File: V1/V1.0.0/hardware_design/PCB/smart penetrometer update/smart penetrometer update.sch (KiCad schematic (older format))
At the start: 25 parts, among them J1 XLR3_Switched, J2 Conn_01x11_Female, U1 4001, U2 DS3231M, U3 Battery_Input, U4 4023, U5 ADS1115IDGS, U6 3v3_Voltage_Regulator, U7 Solar_Input

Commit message: code update
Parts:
- A1: symbol smart-penetrometer-rescue:SD_Card_Module-Charleslabs_Parts-kitest-rescue -> smart-penetrometer-update-rescue:SD_Card_Module-Charleslabs_Parts-kitest-rescue-smart-penetrometer-rescue
- A2: symbol smart-penetrometer-rescue:Arduino_Nano_v3.x-MCU_Module-kitest-rescue -> smart-penetrometer-update-rescue:Arduino_Nano_v3.x-MCU_Module-kitest-rescue-smart-penetrometer-rescue
- U3, U7: symbol smart-penetrometer-rescue:Battery_Input-kitest-kitest-rescue -> smart-penetrometer-update-rescue:Battery_Input-kitest-kitest-rescue-smart-penetrometer-rescue
- U6: symbol smart-penetrometer-rescue:3v3_Voltage_Regulator -> smart-penetrometer-update-rescue:3v3_Voltage_Regulator-smart-penetrometer-rescue
- U?: symbol smart-penetrometer-rescue:DW01 -> smart-penetrometer-update-rescue:DW01-smart-penetrometer-rescue
- U?: symbol smart-penetrometer-rescue:FS8205A -> smart-penetrometer-update-rescue:FS8205A-smart-penetrometer-rescue
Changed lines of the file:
@@
 NoConn ~ 4850 4450
 $Comp
-L smart-penetrometer-rescue:Battery_Input-kitest-kitest-rescue U3
+L smart-penetrometer-update-rescue:Battery_Input-kitest-kitest-rescue-smart-penetrometer-rescue U3
 U 1 1 60A6877D
 P 4200 750
@@
 $EndComp
 $Comp
-L smart-penetrometer-rescue:Arduino_Nano_v3.x-MCU_Module-kitest-rescue A2
+L smart-penetrometer-update-rescue:Arduino_Nano_v3.x-MCU_Module-kitest-rescue-smart-penetrometer-rescue A2
 U 1 1 60A40C30
 P 5350 4150
@@
 $EndComp
 $Comp
-L smart-penetrometer-rescue:SD_Card_Module-Charleslabs_Parts-kitest-rescue A1
+L smart-penetrometer-update-rescue:SD_Card_Module-Charleslabs_Parts-kitest-rescue-smart-penetrometer-rescue A1
 U 1 1 60A4A816
 P 5350 2750
@@
 $EndComp
 $Comp
-L smart-penetrometer-rescue:3v3_Voltage_Regulator U6
+L smart-penetrometer-update-rescue:3v3_Voltage_Regulator-smart-penetrometer-rescue U6
 U 1 1 61FF42DE
 P 2650 2600
@@
 $EndComp
 $Comp
-L smart-penetrometer-rescue:Battery_Input-kitest-kitest-rescue U7
+L smart-penetrometer-update-rescue:Battery_Input-kitest-kitest-rescue-smart-penetrometer-rescue U7
 U 1 1 62051BA4
 P 3400 1950
@@
 $EndComp
 $Comp
-L smart-penetrometer-rescue:DW01 U?
+L smart-penetrometer-update-rescue:DW01-smart-penetrometer-rescue U?
 U 1 1 62805E03
 P 4300 1450
@@
 	4050 900  4050 1200
 $Comp
-L smart-penetrometer-rescue:FS8205A U?
+L smart-penetrometer-update-rescue:FS8205A-smart-penetrometer-rescue U?
 U 1 1 62819888
 P 2600 1250

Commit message: schematic update
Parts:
- removed U1: 4001, kitest:uofsc_logo_1in, symbol 4xxx:4001
- added C? (x2): C_0.047uF, symbol Device:C_Small
- added C?: C_0.47uF, symbol Device:C_Small
- added C? (x2): C_0.1uF, symbol Device:C_Small
- added R? (x2): R_800Ohm, symbol Device:R_Small_US
- added R? (x2): R_1MOhm, symbol Device:R_Small_US
- added U?: ADS1120-PW, Package_SO:TSSOP-16_4.4x5mm_P0.65mm, symbol Analog_ADC:ADS1120-PW
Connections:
- net labels added: Earth
- wire segments 121 -> 147
- no-connect marks 30 -> 31

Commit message: SCHEMATIC UPDAYE
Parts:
- added U?: SRAM(23K256), symbol smart-penetrometer-update-rescue:SRAM(23K256)
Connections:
- net GND: now also U?.4 (VSS)
- net at A2.10 (D7): now also U?.7 (HOLD)
- net at A2.11 (D8): now also U?.1 (CS)
- net at A1.3 (MOSI), A2.14 (D11), U?.16 (DIN): now also U?.5 (SI)
- net at A1.5 (MISO), A2.15 (D12), U?.15 (DOUT/~DRDY): now also U?.2 (SO)
- net at A1.4 (CLK), A2.16 (D13), U?.1 (SCLK): now also U?.6 (SCK)
- net at A1.1 (3V3), A2.30 (VIN), C2.2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: now also U?.8 (VCC)
- no-connect marks 31 -> 29
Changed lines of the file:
@@
 NoConn ~ 4850 4050
 NoConn ~ 4850 4150
-NoConn ~ 4850 4250
-NoConn ~ 4850 4350
 $Comp
 L smart-penetrometer-update-rescue:Battery_Input-kitest-kitest-rescue-smart-penetrometer-rescue U3
@@
 	1    0    0    -1
 $EndComp
-$Comp
-L Analog_ADC:ADS1115IDGS U5
-U 1 1 615B81A7
-P 5150 6300
-F 0 "U5" H 5150 6981 50  0000 C CNN
-F 1 "ADS1115IDGS" H 5150 6890 50  0000 C CNN
-F 2 "Package_SO:TSSOP-10_3x3mm_P0.5mm" H 5150 5800 50  0001 C CNN
-F 3 "http://www.ti.com/lit/ds/symlink/ads1113.pdf" H 5100 5400 50  0001 C CNN
-	1    5150 6300
-	1    0    0    -1
-$EndComp
 Wire Wire Line
 	5550 6300 5950 6300
@@
 U 1 1 6162D30F
 P 6050 3200
-F 0 "R5" H 6118 3246 50  0000 L CNN
-F 1 "R_Small_US" H 6118 3155 50  0000 L CNN
+F 0 "R5" H 6000 3350 50  0000 L CNN
+F 1 "R_Small_US" V 5950 2850 50  0000 L CNN
 F 2 "Resistor_SMD:R_1206_3216Metric" H 6050 3200 50  0001 C CNN
 F 3 "~" H 6050 3200 50  0001 C CNN
@@
 U 1 1 6162E2E0
 P 6150 3200
-F 0 "R6" H 6150 3050 50  0000 L CNN
-F 1 "R_Small_US" H 6218 3155 50  0000 L CNN
+F 0 "R6" H 6100 3350 50  0000 L CNN
+F 1 "R_Small_US" V 6250 2850 50  0000 L CNN
 F 2 "Resistor_SMD:R_1206_3216Metric" H 6150 3200 50  0001 C CNN
 F 3 "~" H 6150 3200 50  0001 C CNN
@@
 U 1 1 6163E9E6
 P 6850 3350
-F 0 "C4" V 6621 3350 50  0000 C CNN
-F 1 "C_Small" V 6712 3350 50  0000 C CNN
+F 0 "C4" V 6950 3450 50  0000 C CNN
+F 1 "C_Small" V 7000 3450 50  0000 C CNN
 F 2 "Capacitor_SMD:C_1206_3216Metric" H 6850 3350 50  0001 C CNN
 F 3 "~" H 6850 3350 50  0001 C CNN
@@
 P 6950 3350
 F 0 "#PWR011" H 6950 3100 50  0001 C CNN
-F 1 "GNDS" V 6955 3222 50  0000 R CNN
+F 1 "GNDS" V 6950 3150 50  0000 R CNN
 F 2 "" H 6950 3350 50  0001 C CNN
 F 3 "" H 6950 3350 50  0001 C CNN
@@
 U 1 1 61FFB484
 P 2900 2850
-F 0 "C2" V 2992 2896 50  0000 L CNN
-F 1 "C_10uF" V 3100 2800 50  0000 L CNN
+F 0 "C2" V 2850 3100 50  0000 L CNN
+F 1 "C_10uF" V 2950 3050 50  0000 L CNN
 F 2 "Capacitor_SMD:C_1206_3216Metric" H 2900 2850 50  0001 C CNN
 F 3 "~" H 2900 2850 50  0001 C CNN
@@
 U 1 1 62002596
 P 2400 3100
-F 0 "D1" H 2450 3200 50  0000 C CNN
-F 1 "D_Zener_Small" H 2400 3300 50  0000 C CNN
+F 0 "D1" H 2800 3050 50  0000 C CNN
+F 1 "D_Zener_Small" H 2800 3100 50  0000 C CNN
 F 2 "Diode_SMD:D_SMC" V 2400 3100 50  0001 C CNN
 F 3 "~" V 2400 3100 50  0001 C CNN
@@
 $EndComp
 Wire Wire Line
-	4700 6300 4700 6950
-Wire Wire Line
 	4700 6950 6400 6950
 Wire Wire Line
@@
 Wire Wire Line
 	4650 6200 4650 7000
-Wire Wire Line
-	4650 7000 6350 7000
 Wire Wire Line
 	6350 7000 6350 5950
@@
 P 3400 1950
 F 0 "U7" H 3658 1984 50  0000 L CNN
-F 1 "Solar_Input" H 3250 2150 50  0000 L CNN
+F 1 "Solar_Input" H 2750 2000 50  0000 L CNN
 F 2 "kitest:Battery_Input" H 3400 1950 50  0001 C CNN
 F 3 "" H 3400 1950 50  0001 C CNN
@@
 P 2300 3100
 F 0 "#PWR0106" H 2300 2850 50  0001 C CNN
-F 1 "GND" H 2305 2927 50  0000 C CNN
+F 1 "GND" H 2300 2950 50  0000 C CNN
 F 2 "" H 2300 3100 50  0001 C CNN
 F 3 "" H 2300 3100 50  0001 C CNN
@@
 P 2300 2850
 F 0 "#PWR0107" H 2300 2600 50  0001 C CNN
-F 1 "GND" H 2305 2677 50  0000 C CNN
+F 1 "GND" H 2300 2700 50  0000 C CNN
 F 2 "" H 2300 2850 50  0001 C CNN
 F 3 "" H 2300 2850 50  0001 C CNN
@@
 U 1 1 6280EF6A
 P 4300 1800
-F 0 "R?" H 4368 1846 50  0000 L CNN
+F 0 "R?" H 4500 1800 50  0000 L CNN
 F 1 "R_Small_US" H 4368 1755 50  0000 L CNN
 F 2 "" H 4300 1800 50  0001 C CNN
@@
 U 1 1 6280FAAE
 P 4350 1100
-F 0 "R?" H 4418 1146 50  0000 L CNN
+F 0 "R?" H 4550 1100 50  0000 L CNN
 F 1 "R_Small_US" H 4418 1055 50  0000 L CNN
 F 2 "" H 4350 1100 50  0001 C CNN
@@
 U 1 1 62819F8F
 P 4200 1000
-F 0 "C?" V 4428 1000 50  0000 C CNN
-F 1 "CP1_Small" V 4337 1000 50  0000 C CNN
+F 0 "C?" V 4300 1000 50  0000 C CNN
+F 1 "CP1_Small" V 4250 1400 50  0000 C CNN
 F 2 "" H 4200 1000 50  0001 C CNN
 F 3 "~" H 4200 1000 50  0001 C CNN
@@
 	2250 4250 2250 4450
 Wire Wire Line
-	2800 3100 3500 3100
+	2800 3100 3450 3100
 Connection ~ 2350 4250
 Connection ~ 2250 4450
@@
 	950  4250 950  4750
 Connection ~ 2250 4250
+$Comp
+L smart-penetrometer-update-rescue:SRAM(23K256) U?
+U 1 1 62EB656F
+P 2500 6900
+F 0 "U?" H 2500 7465 50  0000 C CNN
+F 1 "SRAM(23K256)" H 2500 7374 50  0000 C CNN
+F 2 "" H 2500 6900 50  0001 C CNN
+F 3 "" H 2500 6900 50  0001 C CNN
+	1    2500 6900
+	1    0    0    -1
+$EndComp
+Wire Wire Line
+	2800 6600 3450 6600
+Wire Wire Line
+	3450 6600 3450 3100
+Connection ~ 3450 3100
+Wire Wire Line
+	3450 3100 3500 3100
+$Comp
+L power:GND #PWR?
+U 1 1 62FCEB65
+P 2200 7200
+F 0 "#PWR?" H 2200 6950 50  0001 C CNN
+F 1 "GND" H 2205 7027 50  0000 C CNN
+F 2 "" H 2200 7200 50  0001 C CNN
+F 3 "" H 2200 7200 50  0001 C CNN
+	1    2200 7200
+	1    0    0    -1
+$EndComp
+$Comp
+L Analog_ADC:ADS1115IDGS U5
+U 1 1 615B81A7
+P 5150 6300
+F 0 "U5" H 5150 6981 50  0000 C CNN
+F 1 "ADS1115IDGS" H 5150 6890 50  0000 C CNN
+F 2 "Package_SO:TSSOP-10_3x3mm_P0.5mm" H 5150 5800 50  0001 C CNN
+F 3 "http://www.ti.com/lit/ds/symlink/ads1113.pdf" H 5100 5400 50  0001 C CNN
+	1    5150 6300
+	1    0    0    -1
+$EndComp
+Wire Wire Line
+	4700 6300 4700 6950
+Wire Wire Line
+	4650 7000 6350 7000
+Wire Wire Line
+	4750 4900 4750 6050
+Wire Wire Line
+	4750 6050 3650 6050
+Wire Wire Line
+	3650 6050 3650 7000
+Wire Wire Line
+	3650 7000 2800 7000
+Connection ~ 4750 4900
+Wire Wire Line
+	4700 5000 4700 6000
+Wire Wire Line
+	4700 6000 3700 6000
+Wire Wire Line
+	3700 6000 3700 7200
+Wire Wire Line
+	3700 7200 2800 7200
+Connection ~ 4700 5000
+Wire Wire Line
+	4800 5100 4800 6100
+Wire Wire Line
+	4800 6100 2100 6100
+Wire Wire Line
+	2100 6100 2100 6800
+Wire Wire Line
+	2100 6800 2200 6800
+Connection ~ 4800 5100
+Wire Wire Line
+	2200 6600 2200 5950
+Wire Wire Line
+	2200 5950 4550 5950
+Wire Wire Line
+	4550 5950 4550 4350
+Wire Wire Line
+	4550 4350 4850 4350
+Wire Wire Line
+	2800 6800 3600 6800
+Wire Wire Line
+	3600 6800 3600 5900
+Wire Wire Line
+	3600 5900 4500 5900
+Wire Wire Line
+	4500 5900 4500 4250
+Wire Wire Line
+	4500 4250 4850 4250
 $EndSCHEMATC

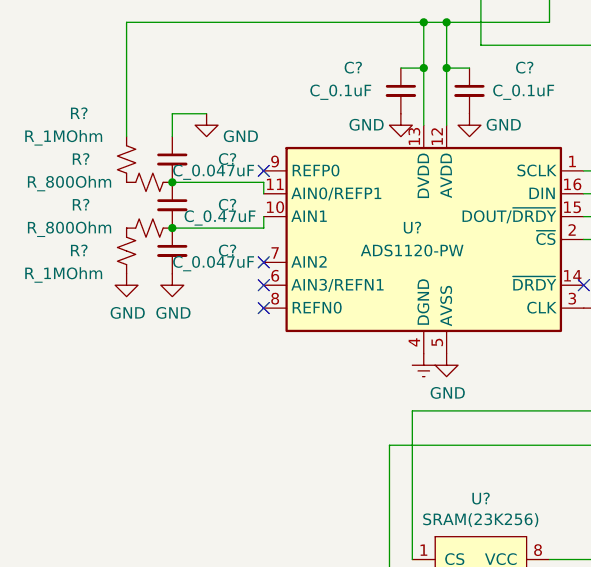
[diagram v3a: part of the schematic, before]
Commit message: schematic update
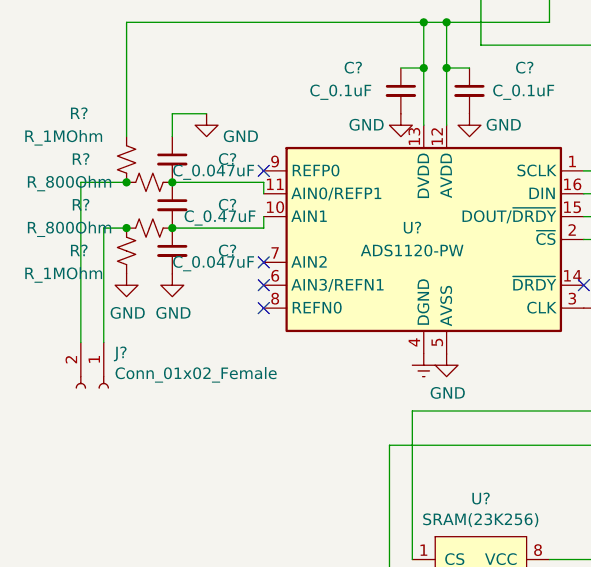
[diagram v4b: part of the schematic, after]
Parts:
- added J?: Conn_01x02_Female, symbol Connector:Conn_01x02_Female
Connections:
- net at R?.2, R?.2: now also J?.2 (Pin_2)
- net at R?.1, R?.2: now also J?.1 (Pin_1)
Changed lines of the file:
@@
 Wire Wire Line
 	4500 4250 4850 4250
+Wire Wire Line
+	950  5150 850  5150
+Wire Wire Line
+	850  5150 850  5650
+Connection ~ 950  5150
+$Comp
+L Connector:Conn_01x02_Female J?
+U 1 1 63030D60
+P 850 5850
+F 0 "J?" V 696 5898 50  0000 L CNN
+F 1 "Conn_01x02_Female" V 787 5898 50  0000 L CNN
+F 2 "" H 850 5850 50  0001 C CNN
+F 3 "~" H 850 5850 50  0001 C CNN
+	1    850  5850
+	0    1    1    0
+$EndComp
+Wire Wire Line
+	950  4950 750  4950
+Wire Wire Line
+	750  4950 750  5650
+Connection ~ 950  4950
 $EndSCHEMATC

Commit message: no change
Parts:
- added C10: C_0.1uF, Capacitor_SMD:C_1206_3216Metric, symbol Device:C_Small
- added C3, C8: C_10uF, Capacitor_SMD:C_1206_3216Metric, symbol Device:C_Small
- added D4: PMEG6045ETP, Diode_SMD:D_SOD-128, symbol Diode:PMEG6045ETP
- added L1: L, Inductor_SMD:L_1206_3216Metric, symbol Device:L
- added R7, R8: R_Small_US, Resistor_SMD:R_1206_3216Metric, symbol Device:R_Small_US
- added U1: LM22676MR-5, Package_SO:TI_SO-PowerPAD-8, symbol Regulator_Switching:LM22676MR-5
- C11, C12, C5, C6, C7, C9: renamed from C?; footprint (none) -> Capacitor_SMD:C_1206_3216Metric
- J3: renamed from J?; footprint (none) -> Connector_PinSocket_2.54mm:PinSocket_1x02_P2.54mm_Horizontal
- R1, R10, R2, R3, R4, R9: renamed from R?; footprint (none) -> Resistor_SMD:R_1206_3216Metric
- U10: renamed from U?; footprint (none) -> smart penetrometer footprints:DUAL_MOSFET(FS8205A)
- U11: renamed from U?; footprint (none) -> smart penetrometer footprints:BATTERY_PROTECTION_IC(DW01A)
- U3, U7: symbol smart-penetrometer-update-rescue:Battery_Input-kitest-kitest-rescue-smart-penetrometer-rescue -> smart-penetrometer-update-rescue:Battery_Input-kitest-kitest-rescue-smart-penetrometer-rescue-smart-penetrometer-update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
- U9: renamed from U?; footprint (none) -> smart penetrometer footprints:23K256T-E&slash_SN
- gave numbers to parts that had none: 1
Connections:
- net GND: now also C10.1, C3.1, D4.2 (A), R8.1, U1.6 (GND)
- net -BATT: now reaches C12.1, U10.2 (S1), U10.3 (S1), U11.6 (GND), U3.2 (Neg)
- net at C1.1, D1.1 (K), U6.1 (VIN): now also C10.2, L1.1, R7.1; no longer J1.3
- net VCC renamed +BATT
- new net: C3.2, J1.3, U1.7 (VIN)
- new net: C8.2, U1.1 (BOOT)
- new net: R7.2, R8.2, U1.4 (FB)
- new net: C8.1, D4.1 (K), L1.2, U1.8 (SW)
- no-connect marks 29 -> 32
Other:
- moved on the sheet: C1, C2, D1, U6
